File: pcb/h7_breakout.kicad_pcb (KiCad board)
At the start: 2 copper layers, 214 x 51 mm, 68 parts, among them J1 USB_B, J10 RJ45_pyControl, J11 RJ45_pyControl, J12 RJ45_pyControl, J13 RJ45_pyControl, J14 RJ45_pyControl, J15 RJ45_pyControl, J16 Conn_01x06_Pin, J2 PJ-037A, J3 SWD_connector, J4 RJ45_pyControl, J5 RJ45_pyControl, J6 RJ45_pyControl, J7 RJ45_pyControl, J8 RJ45_pyControl, J9 RJ45_pyControl, U1 R-78E5.0-1.0, U10 SRV05-4, U11 SRV05-4, U12 SRV05-4, U13 SRV05-4, U14 SRV05-4, U15 SRV05-4, U16 SRV05-4, U17 SRV05-4, U18 SRV05-4, U19 SRV05-4, U2 AMS1117-3.3, U20 SRV05-4, U3 USBLC6-2SC6, U4 STM32H743VIT6, U5 W25Q25PWSSIQ, U6 TBD62083APG, U7 TBD62083APG, U8 TBD62083APG, U9 SRV05-4, Y1 25 MHz, Y2 Crystal

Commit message: PCB v0.2
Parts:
- added FID1: Fiducial, Fiducial:Fiducial_0.75mm_Mask2.25mm, F.Cu at (19.5, 83.0)
- added FID2: Fiducial, Fiducial:Fiducial_0.75mm_Mask2.25mm, F.Cu at (244.5, 82.0)
- added FID3: Fiducial, Fiducial:Fiducial_0.75mm_Mask2.25mm, F.Cu at (261.0, 129.0)
- added J10: Conn_Coaxial, asl_footprints:GCT_RFPC-SMA27-F, F.Cu at (41.5, 126.0)
- added J11: Conn_Coaxial, asl_footprints:GCT_RFPC-SMA27-F, F.Cu at (51.5, 126.0)
- added J12: Conn_Coaxial, asl_footprints:GCT_RFPC-SMA27-F, F.Cu at (61.5, 126.0)
- added J9: Conn_Coaxial, asl_footprints:GCT_RFPC-SMA27-F, F.Cu at (31.5, 126.0)
- added R2: 10 kΩ, Resistor_SMD:R_0603_1608Metric_Pad0.98x0.95mm_HandSolder, F.Cu at (245.5, 91.0)
- added SW1: SW_DPDT_x2, asl_footprints:switch_slide_DPDT, F.Cu at (239.0, 92.0)
- added U5: W25Q25PWSSIQ, Package_SON:WSON-8-1EP_8x6mm_P1.27mm_EP3.4x4.3mm, F.Cu at (202.7, 102.9)
- C11, C12, C7, C8: value 10pF -> 10 pF
- C2, C3: value 10µF -> 10 µF; footprint Capacitor_SMD:C_1206_3216Metric -> Capacitor_SMD:C_1206_3216Metric_Pad1.33x1.80mm_HandSolder
- R1: value 20K -> 10 kΩ; footprint Resistor_SMD:R_1206_3216Metric -> Resistor_SMD:R_0603_1608Metric_Pad0.98x0.95mm_HandSolder
- moved R6 33.8 mm to (45.0, 114.2)
- moved R5 33.8 mm to (45.0, 116.0)
- moved R4 33.8 mm to (45.0, 118.5)
- moved D1 32.9 mm to (40.0, 116.5)
- moved S3 31.3 mm to (28.8, 114.2)
- moved DRA2 27.0 mm to (22.0, 106.5)
- moved H1 27.0 mm to (38.0, 85.0)
- moved H2 27.0 mm to (22.0, 126.0)
- moved S2 26.8 mm to (28.8, 92.2)
- moved D2 14.5 mm to (247.5, 94.2), turned to 180 degrees
- moved J2 12.0 mm to (255.7, 86.0)
- moved S1 12.0 mm to (251.8, 92.2)
- moved C1 12.0 mm to (249.5, 101.0)
- moved C10 12.0 mm to (178.2, 93.0)
- moved C11 12.0 mm to (150.6, 94.2)
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- renumbered D2 to D1, D1 to D2, H3 to H2, H2 to H3, J8 to J13, J9 to J14, J10 to J15, J11 to J16, J12 to J17, J13 to J18, J14 to J19, J15 to J20, J16 to J4, J4 to J5, J5 to J6, J6 to J7, J7 to J8, R2 to R3, R3 to R4, R6 to R5, R5 to R6, R4 to R7, U9 to U10, U10 to U11, U11 to U12, U12 to U13, U13 to U14, U14 to U15, U15 to U16, U16 to U17, U17 to U18, U18 to U19, U19 to U20, U20 to U21, U5 to U6, U6 to U7, U7 to U8, U8 to U9
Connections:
- D2 pad 2: Net-(D1-A) -> Net-(D2-A)
- J2 pad 1: +12V -> Net-(SW1A-B)
- R1 pad 2: Net-(D1-A) -> Net-(R1-Pad2)
- U2 pad 3: VBUS -> +5V
- U4 pad 22: /2_COM_A -> /11_A
- U4 pad 23: /2_C -> /11_B
- U4 pad 34: /11_A -> /2_COM_A
- U4 pad 77: unconnected-(U4-PA15-Pad77) -> /2_C
- U4 pad 81: unconnected-(U4-PD0-Pad81) -> /12_B
- U4 pad 82: unconnected-(U4-PD1-Pad82) -> /12_C
- U4 pad 83: unconnected-(U4-PD2-Pad83) -> /12_A
- U4 pad 85: unconnected-(U4-PD4-Pad85) -> /SMA_1
- U4 pad 86: unconnected-(U4-PD5-Pad86) -> /SMA_2
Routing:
- net /SMA_1: track 0.00 -> 193.5 mm, vias 0 -> 5
- net /SMA_2: track 0.00 -> 172.7 mm, vias 0 -> 3
- net /12_A: track 5.26 -> 135.7 mm, vias 0 -> 5
- net /12_C: track 2.08 -> 131.2 mm, vias 0 -> 7
- net /12_B: track 8.91 -> 131.5 mm, vias 1 -> 6
- net /11_B: track 8.56 -> 110.7 mm, vias 1 -> 6
- net /3_C: track 111.1 -> 180.1 mm, vias 3 -> 5
- net /2_C: track 90.9 -> 159.6 mm, vias 1 -> 5
- net +3.3V: track 537.3 -> 598.5 mm, vias 13 -> 15
- net Net-(U4-PE3): track 86.7 -> 138.1 mm, vias 2 -> 4
- net /USER: track 105.0 -> 156.0 mm, vias 1 -> 0
- net Net-(U4-PC9): track 112.3 -> 160.0 mm
- net Net-(U4-PE11): track 107.9 -> 149.5 mm
- net /RST: track 162.7 -> 203.5 mm
- net /8_C: track 154.6 -> 195.3 mm, vias 4 -> 5
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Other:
- board size 214 x 51 mm -> 253 x 51 mm
- board text added: "1"
- board text added: "8"
- board text added: "pyControl H7 Breakout v0.2 March 2026"
- board text removed: "pyControl H7 Breakout v0.1 Feb 2026"

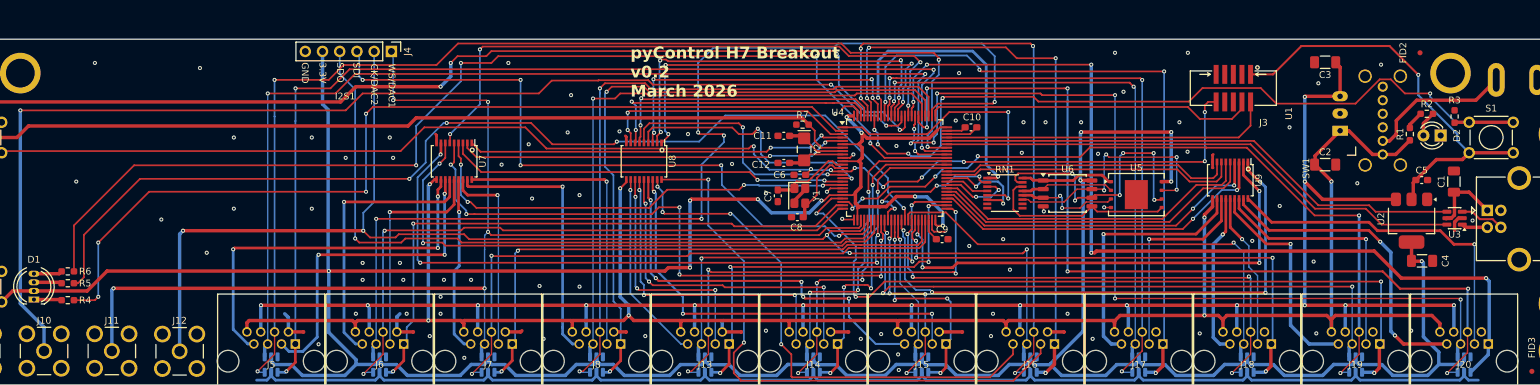
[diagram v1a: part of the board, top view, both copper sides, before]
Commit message: PCB v0.3
don't short the power supply with the on/off switch 🤦
flipped UART4 pins. TX(4_A)/RX(4_B) was PC11(79)/PC10(78), now PC10(78)/PC11(79)
connect Vref to 3.3V so DAC works
change RGB LEDs to 10k
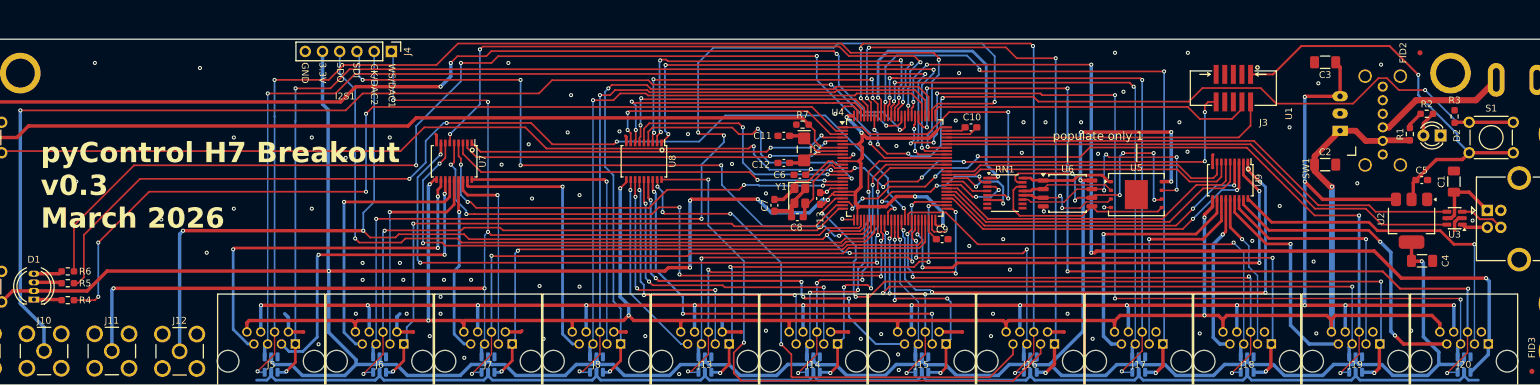
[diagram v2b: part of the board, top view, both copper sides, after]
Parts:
- added C13: 100 nF, Capacitor_SMD:C_0603_1608Metric_Pad1.08x0.95mm_HandSolder, F.Cu at (156.0, 103.5)
- D1: value RGB_LED -> WP154A4SEJ3VBDZGW/CA
- D2: value 12_LED -> 151031VS06000
- H1, H2, H3, H4: value Threaded_Standoff -> 9774130360R
- J10, J11, J12, J9: value Conn_Coaxial -> RFPC-SMA27-F
- R1, R2, R3, R7: value 10 kΩ -> 10 KΩ
- R4, R5: value 91 Ω -> 10 KΩ
- R6: value 6.8Ω -> 10 KΩ
- S1, S2, S3: value TS02-66 -> TS02-66-170-BK-260-LCR-D
- SW1: value SW_DPDT_x2 -> 1825263-1
- U10, U11, U12, U13, U14, U15, U16, U17, U18, U19, U20, U21: value SRV05-4 -> D1213A-04TS-7
- U5: value W25Q25PWSSIQ -> W25Q256JVEIQ
- moved C7 1.49 mm to (149.2, 104.5)
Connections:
- J2 pad 1: Net-(SW1A-B) -> Net-(SW1A-C)
- SW1 pad 1: +12V -> unconnected-(SW1A-A-Pad1)
- SW1 pad 2: Net-(SW1A-B) -> +12V
- SW1 pad 3: GND -> Net-(SW1A-C)
- U4 pad 20: unconnected-(U4-VREF+-Pad20) -> +3.3V
- U4 pad 78: /4_B -> /4_A
- U4 pad 79: /4_A -> /4_B
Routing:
- net Net-(SW1A-B): track 21.6 -> 0.00 mm
- net Net-(SW1A-C): track 0.00 -> 19.6 mm
- net GND: track 255.3 -> 261.1 mm
- net +3.3V: track 598.5 -> 603.6 mm
- net /4_B: track 97.7 -> 95.4 mm
- net /11_A: track 114.5 -> 113.0 mm
- net +12V: track 303.7 -> 302.3 mm
- net /4_A: track 94.8 -> 96.0 mm
- net Net-(U4-PH0): track 12.0 -> 13.0 mm
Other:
- board text added: "populate only 1"
- board text added: "pyControl H7 Breakout v${REVISION} March 2026"
- board text removed: "pyControl H7 Breakout v0.2 March 2026"

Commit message: PCB v0.4
- was 2 layer, now 4 layer board
- was USB type B, now USB type C connector
- was SMA coaxial connectors, now BNC
- was 12 ports, now 10 ports
- added POW_C pins to 2 of the ports
- added8 extra GPIOs, 2 POW pins, and 5V/12V/GND rails on 16 pin terminal block
- 4 user buttons instead of 1
- 4 3mm LEDs instead of single RGB led
- removed SWD connector
- update to KiCAD 10
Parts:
- removed the D1 at (40.0, 116.5)
- removed the J1 at (254.4, 105.2)
- removed the J11 at (51.5, 126.0)
- removed the J12 at (61.5, 126.0)
- removed the J4 at (92.7, 81.8)
- removed the J5 at (75.0, 127.5)
- removed the J6 at (91.0, 127.5)
- added D2: 151031VS06000, LED_THT:LED_D3.0mm, F.Cu at (45.5, 111.1)
- added D3: 151031VS06000, LED_THT:LED_D3.0mm, F.Cu at (45.5, 97.2)
- added D4: 151031VS06000, LED_THT:LED_D3.0mm, F.Cu at (45.5, 118.0)
- added D5: 151031VS06000, LED_THT:LED_D3.0mm, F.Cu at (45.5, 104.2)
- added J2: USB4105-GF-A, Connector_USB:USB_C_Receptacle_GCT_USB4105-xx-A_16P_TopMnt_Horizontal, F.Cu at (266.2, 106.5)
- added J7: 0731000154, asl_footprints:BNC RA Jack, F.Cu at (38.8, 126.5)
- added J8: 0731000154, asl_footprints:BNC RA Jack, F.Cu at (54.8, 126.5)
- added R10: 10 KΩ, Resistor_SMD:R_0603_1608Metric_Pad0.98x0.95mm_HandSolder, F.Cu at (43.0, 118.0)
- added R12: 10 KΩ, Resistor_SMD:R_0603_1608Metric_Pad0.98x0.95mm_HandSolder, F.Cu at (36.5, 104.2)
- added R2: 5.1KΩ, Resistor_SMD:R_0603_1608Metric_Pad0.98x0.95mm_HandSolder, F.Cu at (259.2, 109.5)
- added R4: 5.1KΩ, Resistor_SMD:R_0603_1608Metric_Pad0.98x0.95mm_HandSolder, F.Cu at (259.2, 102.8)
- added R6: 10 KΩ, Resistor_SMD:R_0603_1608Metric_Pad0.98x0.95mm_HandSolder, F.Cu at (36.6, 118.0)
- added R9: 10 KΩ, Resistor_SMD:R_0603_1608Metric_Pad0.98x0.95mm_HandSolder, F.Cu at (36.5, 111.1)
- added S3: TS02-66-170-BK-260-LCR-D, asl_footprints:SW_TH_Tactile_TS02-66, F.Cu at (27.8, 115.8)
- added S4: TS02-66-170-BK-260-LCR-D, asl_footprints:SW_TH_Tactile_TS02-66, F.Cu at (34.2, 113.3)
- added S5: TS02-66-170-BK-260-LCR-D, asl_footprints:SW_TH_Tactile_TS02-66, F.Cu at (34.2, 106.4)
- DRA1, DRA2: value DIN_Rail_Adapter -> 1201578
- J10, J9: value RFPC-SMA27-F -> 0731000154; footprint asl_footprints:GCT_RFPC-SMA27-F -> asl_footprints:BNC RA Jack
- J11: renamed from J14; value RJ45_pyControl -> E5J88-00LJG2-L
- J12: renamed from J15; value RJ45_pyControl -> E5J88-00LJG2-L
- J13: renamed from J16; value RJ45_pyControl -> E5J88-00LJG2-L
- J14: renamed from J17; value RJ45_pyControl -> E5J88-00LJG2-L
- J15: renamed from J18; value RJ45_pyControl -> E5J88-00LJG2-L
- J16: renamed from J19; value RJ45_pyControl -> E5J88-00LJG2-L
- J17: renamed from J20; value RJ45_pyControl -> E5J88-00LJG2-L
- J3: value SWD_connector -> 1803413; footprint asl_footprints:SWD_2x5_socket -> Connector_Phoenix_MC:PhoenixContact_MC_1,5_16-G-3.81_1x16_P3.81mm_Horizontal
- J4: renamed from J7; value RJ45_pyControl -> E5J88-00LJG2-L
- J5: renamed from J8; value RJ45_pyControl -> E5J88-00LJG2-L
- J6: renamed from J13; value RJ45_pyControl -> E5J88-00LJG2-L
- RN1: value 8x33Ω -> 8D33Ω
- U10, U11: moved to F.Cu
- Y2: value Crystal -> 32.768 KHz
- moved R13 117.0 mm to (36.5, 97.2), turned to -90 degrees
- moved J3 115.2 mm to (101.8, 88.4)
- moved U11 48.4 mm to (54.0, 96.8), turned to 180 degrees
- moved J10 45.3 mm to (86.8, 126.5)
- moved J9 39.3 mm to (70.8, 126.5)
- moved U10 31.7 mm to (69.4, 96.8), turned to 180 degrees
- moved R8 18.9 mm to (43.0, 97.2), turned to -90 degrees
- moved S6 15.7 mm to (34.2, 99.5), turned to 180 degrees
- moved C3 15.6 mm to (231.0, 99.0), turned to 0 degrees
- moved C2 15.0 mm to (231.0, 83.5)
- moved R11 10.3 mm to (43.0, 104.2), turned to 90 degrees
- moved R7 7.68 mm to (43.0, 111.1), turned to -90 degrees
- moved U1 6.48 mm to (228.3, 88.8), turned to -90 degrees
- moved U3 6.43 mm to (256.0, 106.4)
- moved C1 5.22 mm to (254.4, 102.8), turned to 180 degrees
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- renumbered C9 to C10, C10 to C11, C11 to C12, C12 to C13, C13 to C8, C8 to C9, D2 to D1, J2 to J1, R6 to R11, R7 to R13, R2 to R3, R3 to R5, R4 to R7, R5 to R8, S3 to S6
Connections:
- J10 pad 1: /SMA_2 -> /6_C
- J11 pad 1: /6_A -> /4_A
- J11 pad 3: /6_PA -> /4_PA
- J11 pad 4: /6_B -> /4_B
- J11 pad 5: /6_C -> /4_C
- J11 pad 7: /6_PB -> /4_PB
- J12 pad 1: /7_A -> /5_A
- J12 pad 3: /7_PA -> /5_PA
- J12 pad 4: /7_B -> /5_B
- J12 pad 5: /7_C -> /5_C
- J12 pad 7: /7_PB -> /5_PB
- J13 pad 1: /8_A -> /6_A
- J13 pad 3: /8_PA -> /6_PA
- J13 pad 4: /8_B -> /6_B
- J13 pad 5: /8_C -> /6_C
- J13 pad 7: /8_PB -> /6_PB
- J14 pad 1: /9_A -> /7_A
- J14 pad 3: /9_PA -> /7_PA
- J14 pad 4: /9_B -> /7_B
- J14 pad 5: /9_C -> /7_C
- J14 pad 7: /9_PB -> /7_PB
- J15 pad 1: /10_A -> /8_A
- J15 pad 3: /10_PA -> /8_PA
- J15 pad 4: /10_B -> /8_B
- J15 pad 5: /10_C -> /8_C
- J15 pad 7: /10_PB -> /8_PB
- J16 pad 1: /11_A -> /9_A
- J16 pad 3: /11_PA -> /9_PA
- J16 pad 4: /11_B -> /9_B
- J16 pad 5: /11_C -> /9_C
- J16 pad 7: /11_PB -> /9_PB
- J17 pad 1: /12_A -> /10_A
- J17 pad 3: /12_PA -> /10_PA
- J17 pad 4: /12_B -> /10_B
- J17 pad 5: /12_C -> /10_C
- J17 pad 7: /12_PB -> /10_PB
- J3 pad 1: +3.3V -> GND
- J3 pad 10: /RST -> /D3
- J3 pad 2: /SWDIO -> +5V
- J3 pad 3: GND -> +12V
- J3 pad 4: /SWCLK -> GND
- J3 pad 5: GND -> /P1
- J3 pad 6: unconnected-(J3-SWO/TDO-Pad6) -> /P2
- J3 pad 7: unconnected-(J3-KEY-Pad7) -> GND
- J3 pad 8: unconnected-(J3-NC/TDI-Pad8) -> /D1
- J3 pad 9: GND -> /D2
- J4 pad 1: /3_A -> /1_A
- J4 pad 3: /3_PA -> /1_PA
- J4 pad 4: /3_B -> /1_B
- J4 pad 5: /3_C -> /1_C
- J4 pad 7: /3_PB -> /1_PB
- J5 pad 1: /4_A -> /2_A
- J5 pad 3: /4_PA -> /2_PA
- J5 pad 4: /4_B -> /2_B
- J5 pad 5: /4_C -> /2_PC
- J5 pad 7: /4_PB -> /2_PB
- J6 pad 1: /5_A -> /3_A
- J6 pad 3: /5_PA -> /3_PA
- J6 pad 4: /5_B -> /3_B
- J6 pad 5: /5_C -> /3_PC
- J6 pad 7: /5_PB -> /3_PB
- J9 pad 1: /SMA_1 -> /1_C
- R11 pad 2: /LED_2 -> Net-(D5-K)
- R7 pad 1: /LED_1 -> Net-(D2-K)
- R8 pad 1: /LED_3 -> Net-(D3-K)
- U10 pad 1: /1_A -> /D1
- U10 pad 3: /1_B -> /D2
- U10 pad 4: /1_C -> /D3
- U10 pad 6: unconnected-(U10-IO4-Pad6) -> /D4
- U11 pad 1: /2_A -> /D5
- U11 pad 3: /2_B -> /D6
- U11 pad 4: /2_C -> /D7
- U11 pad 6: unconnected-(U11-IO4-Pad6) -> /D8
- U12 pad 1: /3_A -> /1_A
- U12 pad 3: /3_B -> /1_B
- U12 pad 4: /3_C -> /1_C
- U13 pad 1: /4_A -> /2_A
- U13 pad 3: /4_B -> /2_B
- U13 pad 4: /4_C -> unconnected-(U13-IO3-Pad4)
- U14 pad 1: /5_A -> /3_A
- U14 pad 3: /5_B -> /3_B
- U14 pad 4: /5_C -> unconnected-(U14-IO3-Pad4)
- U15 pad 1: /6_A -> /4_A
- U15 pad 3: /6_B -> /4_B
- U15 pad 4: /6_C -> /4_C
- U16 pad 1: /7_A -> /5_A
- U16 pad 3: /7_B -> /5_B
- U16 pad 4: /7_C -> /5_C
- U17 pad 1: /8_A -> /6_A
- U17 pad 3: /8_B -> /6_B
- U17 pad 4: /8_C -> /6_C
- U18 pad 1: /9_A -> /7_A
- U18 pad 3: /9_B -> /7_B
- U18 pad 4: /9_C -> /7_C
- U19 pad 1: /10_A -> /8_A
- U19 pad 3: /10_B -> /8_B
- U19 pad 4: /10_C -> /8_C
- U20 pad 1: /11_A -> /9_A
- U20 pad 3: /11_B -> /9_B
- U20 pad 4: /11_C -> /9_C
- U21 pad 1: /12_A -> /10_A
- U21 pad 3: /12_B -> /10_B
- U21 pad 4: /12_C -> /10_C
- U4 pad 15: /6_COM_A -> /4_COM_A
- U4 pad 16: /7_COM_B -> /5_COM_B
- U4 pad 17: /3_COM_A -> /1_COM_A
- U4 pad 18: /3_COM_B -> /1_COM_B
- U4 pad 22: /11_A -> /D1
- U4 pad 23: /11_B -> /D2
- U4 pad 24: /2_A -> /10_A
- U4 pad 25: /2_B -> /10_B
- U4 pad 28: /3_C -> /1_C
- U4 pad 29: /8_C -> /6_C
- U4 pad 3: /5_COM_B -> /3_COM_B
- U4 pad 30: Net-(J4-Pin_3) -> /D3
- U4 pad 31: Net-(J4-Pin_4) -> /D4
- U4 pad 32: /1_COM_A -> /X_COM_A
- U4 pad 33: /1_COM_B -> /X_COM_B
- U4 pad 34: /2_COM_A -> /3_COM_C
- U4 pad 35: /11_C -> /9_C
- U4 pad 37: /7_B -> /5_B
- U4 pad 38: /7_A -> /5_A
- U4 pad 39: /7_C -> /5_C
- U4 pad 4: /4_COM_A -> /2_COM_A
- U4 pad 40: /12_COM_A -> /10_COM_A
- U4 pad 42: /10_C -> /8_C
- U4 pad 43: /10_B -> /8_B
- U4 pad 44: /10_A -> /8_A
- U4 pad 45: /12_COM_B -> /10_COM_B
- U4 pad 46: /3_A -> /1_A
- U4 pad 47: /3_B -> /1_B
- U4 pad 5: /4_COM_B -> /2_COM_B
- U4 pad 51: /5_B -> /3_B
- U4 pad 52: /5_A -> /3_A
- U4 pad 53: /5_C -> /D8
- U4 pad 54: /11_COM_A -> /9_COM_A
- U4 pad 55: /11_COM_B -> /9_COM_B
- U4 pad 56: /10_COM_A -> /8_COM_A
- U4 pad 57: /10_COM_B -> /8_COM_B
- U4 pad 61: /9_COM_A -> /7_COM_A
- U4 pad 62: /9_COM_B -> /7_COM_B
- U4 pad 63: /6_A -> /4_A
- U4 pad 64: /6_B -> /4_B
- U4 pad 65: /6_C -> /4_C
- U4 pad 67: /1_C -> Net-(S3-in1)
- U4 pad 68: /1_A -> /9_A
- U4 pad 69: /1_B -> /9_B
- U4 pad 72: /SWDIO -> /D5
- U4 pad 76: /SWCLK -> /D6
- U4 pad 77: /2_C -> /D7
- U4 pad 78: /4_A -> /2_A
- U4 pad 79: /4_B -> /2_B
- U4 pad 80: /4_C -> Net-(S5-in1)
- U4 pad 81: /12_B -> Net-(S4-in1)
- U4 pad 82: /12_C -> /10_C
- U4 pad 83: /12_A -> Net-(U4-PD2)
- U4 pad 84: /2_COM_B -> /2_COM_C
- U4 pad 87: /8_COM_A -> /6_COM_A
- U4 pad 88: /8_COM_B -> /6_COM_B
- U4 pad 89: /9_C -> /7_C
- U4 pad 90: /9_B -> /7_B
- U4 pad 91: /9_A -> /7_A
- U4 pad 93: /7_COM_A -> /5_COM_A
- U4 pad 95: /8_A -> /6_A
- U4 pad 96: /8_B -> /6_B
- U4 pad 97: /6_COM_B -> /4_COM_B
- U4 pad 98: /5_COM_A -> /3_COM_A
- U7 pad 1: /4_COM_A -> /2_COM_A
- U7 pad 11: /1_PB -> /P2
- U7 pad 12: /1_PA -> /P1
- U7 pad 13: /2_PB -> /2_PC
- U7 pad 14: /2_PA -> /3_PC
- U7 pad 15: /3_PB -> /1_PB
- U7 pad 16: /3_PA -> /1_PA
- U7 pad 17: /4_PB -> /2_PB
- U7 pad 18: /4_PA -> /2_PA
- U7 pad 2: /4_COM_B -> /2_COM_B
- U7 pad 3: /3_COM_A -> /1_COM_A
- U7 pad 4: /3_COM_B -> /1_COM_B
- U7 pad 5: /2_COM_A -> /3_COM_C
- U7 pad 6: /2_COM_B -> /2_COM_C
- U7 pad 7: /1_COM_A -> /X_COM_A
- U7 pad 8: /1_COM_B -> /X_COM_B
- U8 pad 1: /8_COM_A -> /6_COM_A
- U8 pad 11: /5_PB -> /3_PB
- U8 pad 12: /5_PA -> /3_PA
- U8 pad 13: /6_PB -> /4_PB
- U8 pad 14: /6_PA -> /4_PA
- U8 pad 15: /7_PB -> /5_PB
- U8 pad 16: /7_PA -> /5_PA
- U8 pad 17: /8_PB -> /6_PB
- U8 pad 18: /8_PA -> /6_PA
- U8 pad 2: /8_COM_B -> /6_COM_B
- U8 pad 3: /7_COM_A -> /5_COM_A
- U8 pad 4: /7_COM_B -> /5_COM_B
- U8 pad 5: /6_COM_A -> /4_COM_A
- U8 pad 6: /6_COM_B -> /4_COM_B
- U8 pad 7: /5_COM_A -> /3_COM_A
- U8 pad 8: /5_COM_B -> /3_COM_B
- U9 pad 1: /12_COM_A -> /10_COM_A
- U9 pad 11: /9_PB -> /7_PB
- U9 pad 12: /9_PA -> /7_PA
- U9 pad 13: /10_PB -> /8_PB
- U9 pad 14: /10_PA -> /8_PA
- U9 pad 15: /11_PB -> /9_PB
- U9 pad 16: /11_PA -> /9_PA
- U9 pad 17: /12_PB -> /10_PB
- U9 pad 18: /12_PA -> /10_PA
- U9 pad 2: /12_COM_B -> /10_COM_B
- U9 pad 3: /11_COM_A -> /9_COM_A
- U9 pad 4: /11_COM_B -> /9_COM_B
- U9 pad 5: /10_COM_A -> /8_COM_A
- U9 pad 6: /10_COM_B -> /8_COM_B
- U9 pad 7: /9_COM_A -> /7_COM_A
- U9 pad 8: /9_COM_B -> /7_COM_B
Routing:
- net +3.3V: track 603.6 -> 45.4 mm, vias 15 -> 23
- net GND: track 261.1 -> 80.4 mm, vias 87 -> 29
- net /3_C: track 180.1 -> 0.00 mm, vias 5 -> 0
- net Net-(U4-PD2): track 0.00 -> 177.6 mm, vias 0 -> 4
- net Net-(S4-in1): track 0.00 -> 175.9 mm, vias 0 -> 4
- net Net-(S3-in1): track 0.00 -> 173.5 mm, vias 0 -> 4
- net Net-(S5-in1): track 0.00 -> 163.8 mm, vias 0 -> 1
- net /D8: track 0.00 -> 163.3 mm, vias 0 -> 4
- net /2_C: track 159.6 -> 0.00 mm, vias 5 -> 0
- net /D5: track 0.00 -> 142.2 mm, vias 0 -> 4
- net /D6: track 0.00 -> 140.1 mm, vias 0 -> 4
- net /D7: track 0.00 -> 140.1 mm, vias 0 -> 4
- net /12_A: track 135.7 -> 0.00 mm, vias 5 -> 0
- net /12_B: track 131.5 -> 0.00 mm, vias 6 -> 0
- net /12_C: track 131.2 -> 0.00 mm, vias 7 -> 0
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- added copper zone on In2.Cu, net +3.3V
- added copper zone on In1.Cu, net GND
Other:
- copper layers 2 -> 4
- board text added: "12V"
- board text added: "5V"
- board text added: "BOOT"
- board text added: "D1"
- board text added: "D2"
- board text added: "D3"
- board text added: "D4"
- board text added: "D5"
- board text added: "D6"
- board text added: "D7"
- board text added: "D8"
- board text added: "P1"
- board text added: "P2"
- board text added: "USER"
- board text added: "populate 1 only"
- board text added: "pyControl H7 Breakout"
- board text added: "v${REVISION} April 2026"
- board text removed: "3.3V"
- board text removed: "CK/DAC2"
- board text removed: "GND"
- board text removed: "I2S1"
- board text removed: "SDI"
- board text removed: "SDO"
- board text removed: "USR"
- board text removed: "WS/DAC1"
- board text removed: "populate only 1"
- board text removed: "pyControl H7 Breakout v${REVISION} March 2026"

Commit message: PCB v0.5
- connect USB-C shield ground
- connect A6/B6 and A7/B7 on USB-C
- connect C13 to ground
- use 5.1K resistors for everything
- make DC-DC converter pads smaller
- added QR code
- make GPIO labels larger and put on bottom side as well
- shift reset button to bottom right corner
- removed 2 of standoffs. shifted other two to be in vertical center of the board
- DIN connectors are now vertically centered
- added JST SH connector for I2C
- shifted terminal block up so it overhangs board (will stick out case)
- shifted dc jack and on off switch and dfu button and power LED
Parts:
- removed H3, H4: 9774130360R, asl_footprints:standoff_nut
- added J8: Conn_01x04_Socket, Connector_JST:JST_SH_SM04B-SRSS-TB_1x04-1MP_P1.00mm_Horizontal, F.Cu at (25.3, 127.7)
- added R10: 5.1KΩ, Resistor_SMD:R_0603_1608Metric_Pad0.98x0.95mm_HandSolder, F.Cu at (41.2, 108.8)
- added R14: 5.1KΩ, Resistor_SMD:R_0603_1608Metric_Pad0.98x0.95mm_HandSolder, F.Cu at (39.8, 115.8)
- added R15: 5.1KΩ, Resistor_SMD:R_0603_1608Metric_Pad0.98x0.95mm_HandSolder, F.Cu at (39.8, 112.2)
- added R17: 5.1KΩ, Resistor_SMD:R_0603_1608Metric_Pad0.98x0.95mm_HandSolder, F.Cu at (41.2, 102.2)
- added R4: 5.1KΩ, Resistor_SMD:R_0603_1608Metric_Pad0.98x0.95mm_HandSolder, F.Cu at (241.8, 92.2)
- added R5: 5.1KΩ, Resistor_SMD:R_0603_1608Metric_Pad0.98x0.95mm_HandSolder, F.Cu at (241.8, 94.2)
- R1: value 10 KΩ -> 5.1KΩ
- R11: renamed from R8; value 10 KΩ -> 5.1KΩ
- R12: renamed from R9; value 10 KΩ -> 5.1KΩ
- R13: renamed from R10; value 10 KΩ -> 5.1KΩ
- R16: renamed from R11; value 10 KΩ -> 5.1KΩ
- R18: renamed from R12; value 10 KΩ -> 5.1KΩ
- R19: renamed from R13; value 10 KΩ -> 5.1KΩ
- R2: renamed from R3; value 10 KΩ -> 5.1KΩ
- R7: renamed from R5; value 10 KΩ -> 5.1KΩ
- R8: renamed from R6; value 10 KΩ -> 5.1KΩ
- R9: renamed from R7; value 10 KΩ -> 5.1KΩ
- moved S2 242.7 mm to (268.2, 127.0), turned to 180 degrees
- moved H1 195.0 mm to (232.0, 105.0)
- moved C6 108.8 mm to (260.2, 118.0), turned to 90 degrees
- moved H2 39.1 mm to (55.0, 105.0)
- moved R7 21.6 mm to (229.5, 83.2), turned to 90 degrees
- moved FID2 19.8 mm to (224.8, 81.5), turned to 90 degrees
- moved S1 18.0 mm to (233.8, 92.2), turned to 90 degrees
- moved C2 16.2 mm to (227.2, 99.2)
- moved FID3 16.2 mm to (257.2, 113.2), turned to 90 degrees
- moved C1 11.4 mm to (265.2, 99.2), turned to 0 degrees
- moved SW1 11.3 mm to (249.8, 88.7)
- moved C3 8.27 mm to (239.2, 99.5), turned to 180 degrees
- moved D1 6.82 mm to (244.3, 88.7)
- moved R2 6.45 mm to (241.8, 96.2), turned to 180 degrees
- moved U1 4.98 mm to (227.7, 93.7), turned to 90 degrees
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- renumbered J7 to J1, J5 to J10, J6 to J11, J11 to J12, J12 to J13, J13 to J14, J14 to J15, J15 to J16, J16 to J17, J17 to J18, J8 to J2, J9 to J3, J10 to J4, J1 to J5, J2 to J6, J3 to J7, J4 to J9, R2 to R3, R4 to R6
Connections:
- net /SMA_1 renamed /BNC_1
- net /SMA_2 renamed /BNC_2
- J6 pad SH: (no net) -> GND
- R13 pad 1: Net-(U4-PD2) -> Net-(R13-Pad1)
- R2 pad 2: Net-(D1-A) -> Net-(R2-Pad2)
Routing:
- net /1_A: track 82.7 -> 170.8 mm
- net /1_B: track 88.3 -> 170.5 mm
- net /BOOT: track 103.9 -> 84.5 mm
- net Net-(SW1A-C): track 19.6 -> 7.92 mm
- net /RST: track 141.9 -> 131.8 mm, vias 4 -> 6
- net /USER: track 146.8 -> 136.8 mm, vias 1 -> 0
- net +5V: track 250.6 -> 260.1 mm
- net Net-(U4-PE3): track 144.1 -> 138.8 mm
- net +12V: track 307.9 -> 312.9 mm, vias 4 -> 5
- net /BNC_2: track 150.1 -> 145.3 mm
- net Net-(U4-PD2): track 177.6 -> 172.9 mm
- net /D1: track 108.0 -> 112.6 mm
- net Net-(S4-in1): track 175.9 -> 171.5 mm
- net /D2: track 108.9 -> 113.3 mm
- net /D4: track 123.7 -> 128.0 mm
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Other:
- board size 253 x 51 mm -> 253 x 52 mm
- board text added: "12"
- board text added: "5"
- board text added: "BLU"
- board text added: "DAC 1"
- board text added: "DAC 2"
- board text added: "GRN"
- board text added: "I2C 2"
- board text added: "RED"
- board text added: "RESET"
- board text added: "YLW"
- board text added: "v${REVISION} May 2026"
- board text removed: "RST"
- board text removed: "v${REVISION} April 2026"

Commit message: PCB v0.6
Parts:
- removed the R15 at (39.8, 112.2)
- removed the R2 at (241.8, 96.2)
- removed the R4 at (241.8, 92.2)
- removed the R5 at (241.8, 94.2)
- added R10: 5.1KΩ, Resistor_SMD:R_0603_1608Metric_Pad0.98x0.95mm_HandSolder, F.Cu at (41.4, 94.7)
- added R12: 5.1KΩ, Resistor_SMD:R_0603_1608Metric_Pad0.98x0.95mm_HandSolder, F.Cu at (43.2, 115.4)
- added R7: 5.1KΩ, Resistor_SMD:R_0603_1608Metric_Pad0.98x0.95mm_HandSolder, F.Cu at (41.7, 108.7)
- D3: value 151031VS06000 -> 151031SS06000
- D4: value 151031VS06000 -> 151033BS03000
- D5: value 151031VS06000 -> 151031YS05900
- R1, R13: value 5.1KΩ -> 20K
- moved R14 14.2 mm to (40.1, 101.6), turned to 90 degrees
- moved S1 3.95 mm to (235.6, 88.7)
- moved R1 3.36 mm to (243.1, 92.2), turned to 180 degrees
- moved R6 2.87 mm to (40.1, 108.7)
- moved R8 1.93 mm to (43.2, 108.7)
- moved R13 1.40 mm to (41.7, 115.4)
- moved R16 0.77 mm to (41.7, 101.6)
- moved R15 0.67 mm to (43.2, 101.6)
- moved J5 0.64 mm to (256.4, 84.8)
- renumbered R12 to R11, R16 to R15, R17 to R16, R18 to R17, R19 to R18, R3 to R2, R6 to R3, R7 to R4, R8 to R5, R9 to R6, R10 to R8, R11 to R9
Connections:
- J6 pad A6: unconnected-(J6-D+-PadA6) -> Net-(J6-D+-PadA6)
- J6 pad A7: unconnected-(J6-D--PadA7) -> Net-(J6-D--PadA7)
- J6 pad B6: Net-(J6-D+-PadB6) -> Net-(J6-D+-PadA6)
- J6 pad B7: Net-(J6-D--PadB7) -> Net-(J6-D--PadA7)
- R1 pad 2: Net-(R1-Pad2) -> Net-(D1-A)
- R13 pad 1: Net-(R13-Pad1) -> Net-(R12-Pad2)
- R13 pad 2: Net-(D4-K) -> Net-(U4-PD2)
- R14 pad 1: Net-(R14-Pad1) -> Net-(U4-PC9)
- R14 pad 2: Net-(R13-Pad1) -> Net-(D5-K)
- U3 pad 1: Net-(J6-D--PadB7) -> Net-(J6-D--PadA7)
- U3 pad 3: Net-(J6-D+-PadB6) -> Net-(J6-D+-PadA6)
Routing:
- net Net-(J6-D+-PadA6): track 0.00 -> 8.66 mm
- net Net-(J6-D--PadA7): track 0.00 -> 7.88 mm
- net Net-(J6-D+-PadB6): track 5.54 -> 0.00 mm
- net Net-(J6-D--PadB7): track 5.39 -> 0.00 mm
- net Net-(R13-Pad1): track 3.25 -> 0.00 mm
- net Net-(R4-Pad1): track 2.10 -> 0.00 mm
- net Net-(R2-Pad2): track 2.00 -> 0.00 mm
- net Net-(R1-Pad2): track 1.87 -> 0.00 mm
- net Net-(R14-Pad1): track 1.68 -> 0.00 mm
- net Net-(D3-K): track 2.71 -> 4.31 mm
- net Net-(U4-PE11): track 142.3 -> 143.9 mm
- net Net-(R12-Pad2): track 0.00 -> 1.52 mm
- net Net-(U4-PC9): track 165.0 -> 166.5 mm
- net Net-(D5-K): track 4.29 -> 5.68 mm
- net Net-(U4-PD2): track 172.9 -> 174.3 mm
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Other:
- board text added: "10"
- board text added: "2"
- board text added: "3"
- board text added: "4"
- board text added: "6"
- board text added: "7"
- board text added: "9"
- board text added: "v${REVISION} June 2026"
- board text removed: "v${REVISION} May 2026"
